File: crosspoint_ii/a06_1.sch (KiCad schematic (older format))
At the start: 44 parts, among them U6001 74HC27, U6002 74HC02, U6003 74HC27, U6004 74LVC07, U6005 74HC02, U6006 74HC04, U6007 74HC27, U6008 74HC27, U6009 74HC02, U6010 74HC04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

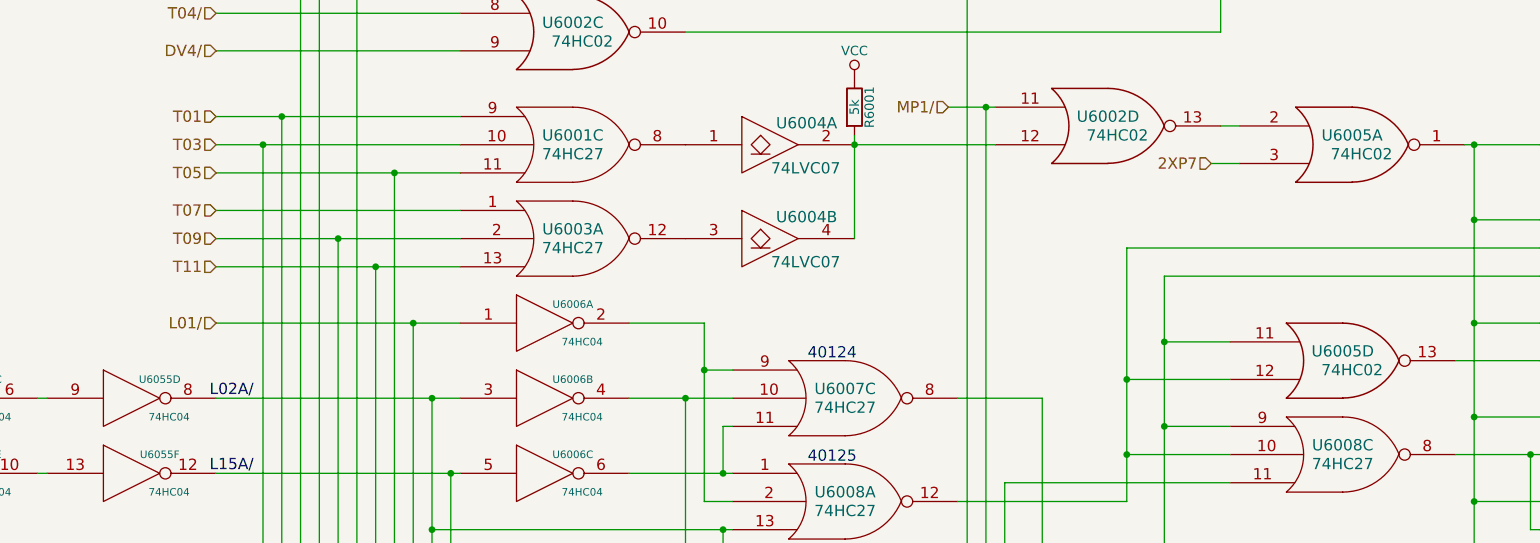
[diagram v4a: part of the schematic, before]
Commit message: Added the final four bit module. All 16 bits of the central/special registers are present. We're stuck at address 0 because TC is using RAD, which needs to be translated into RG or RZ by module 12
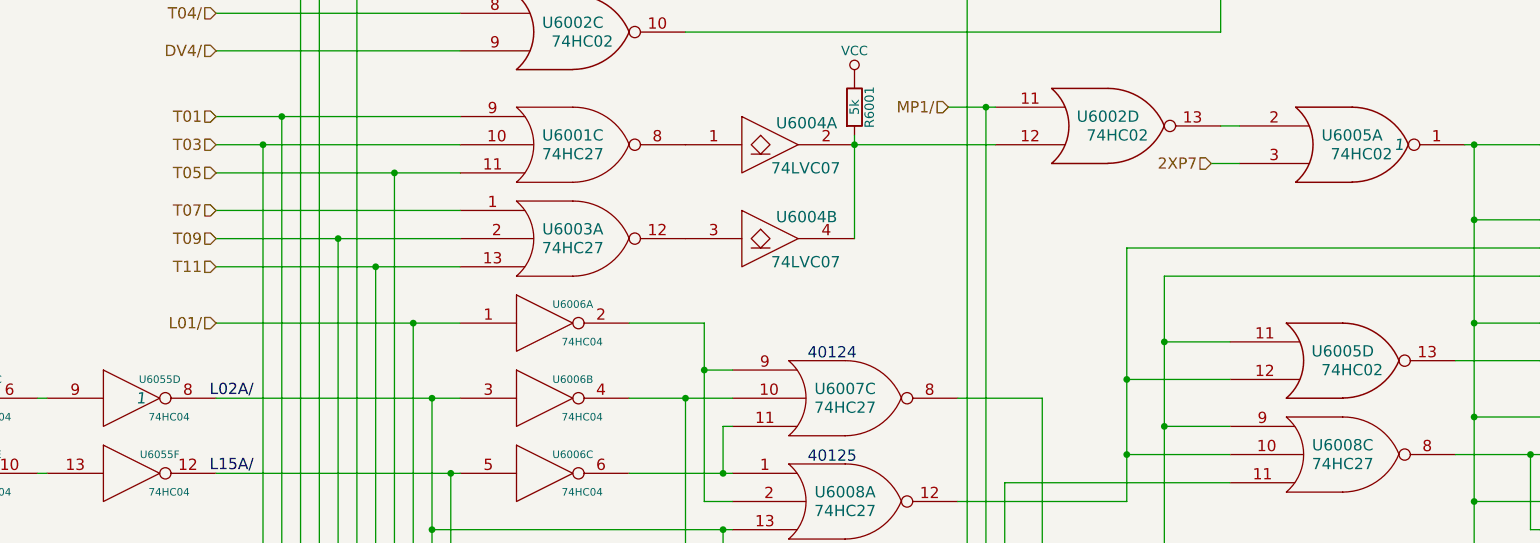
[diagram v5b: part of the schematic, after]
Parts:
- U6005, U6055: Initial (none) -> 1
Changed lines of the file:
@@
 F 2 "" H 9700 3150 60  0000 C CNN
 F 3 "" H 9700 3150 60  0000 C CNN
+F 4 "1" H 9950 3150 60  0000 C CIN "Initial"
 	1    9700 3150
 	1    0    0    -1
@@
 F 2 "" H 3200 4500 60  0000 C CNN
 F 3 "" H 3200 4500 60  0000 C CNN
+F 4 "1" H 3250 4500 60  0000 C CIN "Initial"
 	4    3200 4500
 	1    0    0    -1

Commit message: Added in WHOMP, whatever it is
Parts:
- added U6051: 74HC4002, symbol 74HC4002
- added unit 2 of U6056
- added U6057: 74HC02, symbol 74HC02
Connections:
- net CLXC: now also U6057.3
- net DVXP1: now also U6051.9
- net GND: now also U6051.7 (GND), U6056.7 (GND), U6057.7 (GND)
- net VCC: now also U6051.14 (VCC), U6056.14 (VCC), U6057.14 (VCC)
- new net GOJAM: U6051.10
- new net NISQ: U6051.11
- new net WHOMP: U6051.13, U6057.2
- new net WHOMP/: U6051.12, U6056.3, U6057.1
- new net WHOMPA: U6056.4
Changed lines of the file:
@@
 Connection ~ 12850 12050
-Wire Wire Line
-	11400 2050 11400 1950
-Wire Wire Line
-	11400 1950 11500 1950
-Text HLabel 11500 1950 2    60   Output ~ 0
-DVXP1
 Wire Wire Line
 	6750 6600 6750 6300
@@
 Wire Wire Line
 	16950 6050 16950 6150
-Connection ~ 11400 2050
 Connection ~ 12850 2050
 Wire Wire Line
@@
 Wire Wire Line
 	13200 3700 11900 3700
+Text Label 11350 2050 0    60   ~ 0
+DVXP1
+$Comp
+L 74HC02 U6057
+U 1 1 56AE107E
+P 19700 5750
+F 0 "U6057" H 19700 5800 60  0000 C CNN
+F 1 "74HC02" H 19750 5700 60  0000 C CNN
+F 2 "" H 19700 5750 60  0000 C CNN
+F 3 "" H 19700 5750 60  0000 C CNN
+F 4 "1" H 19950 5750 60  0000 C CIN "Initial"
+	1    19700 5750
+	1    0    0    -1
+$EndComp
+Wire Wire Line
+	20300 5750 20300 5500
+Wire Wire Line
+	20300 5500 19100 5300
+Wire Wire Line
+	19100 5300 19100 5200
+Wire Wire Line
+	20300 5050 20300 5300
+Wire Wire Line
+	20300 5300 19100 5500
+Wire Wire Line
+	19100 5500 19100 5650
+$Comp
+L 74HC4002 U6051
+U 2 1 56AE2757
+P 19700 5050
+F 0 "U6051" H 19700 5100 60  0000 C CNN
+F 1 "74HC4002" H 19750 5000 47  0000 C CNN
+F 2 "" H 19700 5050 60  0000 C CNN
+F 3 "" H 19700 5050 60  0000 C CNN
+	2    19700 5050
+	1    0    0    -1
+$EndComp
+Wire Wire Line
+	17550 7350 17550 7150
+Wire Wire Line
+	17550 7150 18850 7150
+Wire Wire Line
+	18850 7150 18850 5850
+Wire Wire Line
+	18850 5850 19100 5850
+Connection ~ 17550 7350
+Wire Wire Line
+	19100 4900 16850 4900
+Connection ~ 16850 4900
+Text HLabel 19000 5000 0    60   Input ~ 0
+GOJAM
+Wire Wire Line
+	19000 5000 19100 5000
+Text HLabel 19000 5100 0    60   Input ~ 0
+NISQ
+Wire Wire Line
+	19000 5100 19100 5100
+Wire Wire Line
+	20300 5050 20550 5050
+Connection ~ 20300 5050
+Text HLabel 20550 5050 2    60   Output ~ 0
+WHOMP
+Wire Wire Line
+	20300 5750 21000 5750
+Connection ~ 20300 5750
+$Comp
+L 74HC04 U6056
+U 2 1 56AEA36B
+P 21450 5750
+F 0 "U6056" H 21600 5850 40  0000 C CNN
+F 1 "74HC04" H 21650 5650 40  0000 C CNN
+F 2 "" H 21450 5750 60  0000 C CNN
+F 3 "" H 21450 5750 60  0000 C CNN
+	2    21450 5750
+	1    0    0    -1
+$EndComp
+Wire Wire Line
+	21900 5750 22000 5750
+Text HLabel 22000 5750 2    60   Output ~ 0
+WHOMPA
+Text Label 20800 5750 2    60   ~ 0
+WHOMP/
 $EndSCHEMATC

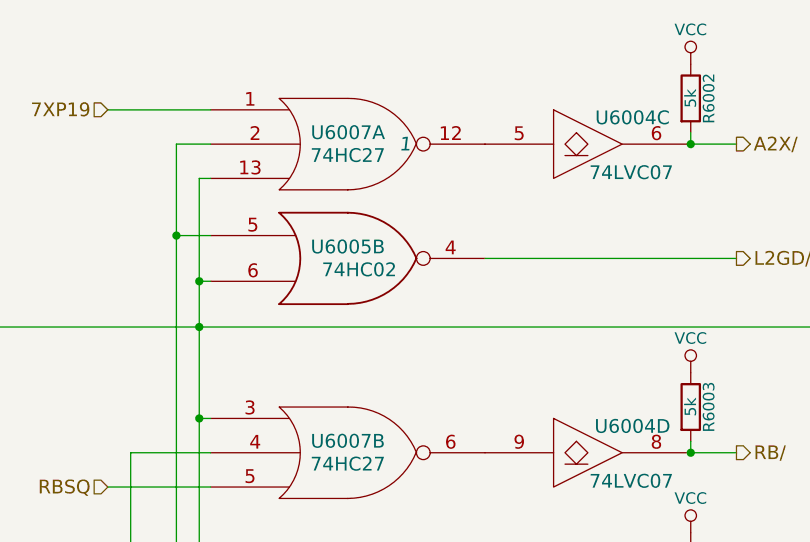
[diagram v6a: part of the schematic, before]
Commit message: Added and tied in module 12, parity & s register
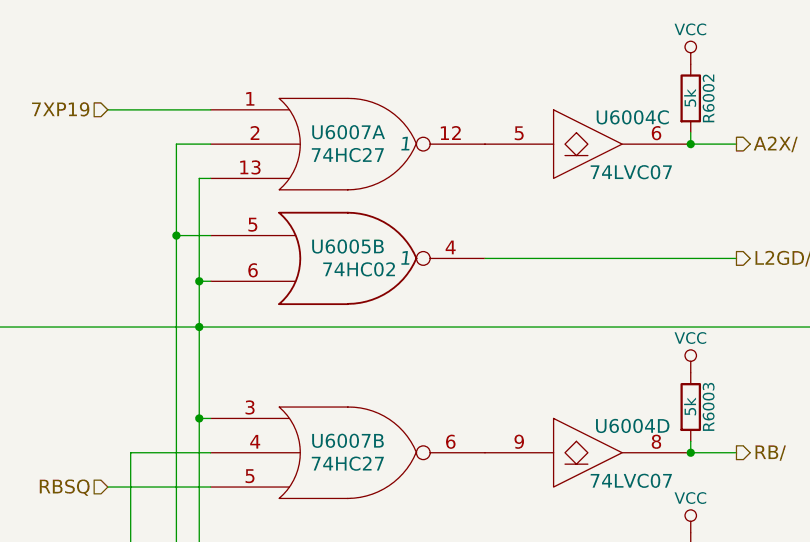
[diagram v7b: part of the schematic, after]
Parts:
- U6005: Initial (none) -> 1
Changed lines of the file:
@@
 F 2 "" H 13500 1750 60  0000 C CNN
 F 3 "" H 13500 1750 60  0000 C CNN
+F 4 "1" H 13750 1750 60  0000 C CIN "Initial"
 	2    13500 1750
 	1    0    0    -1

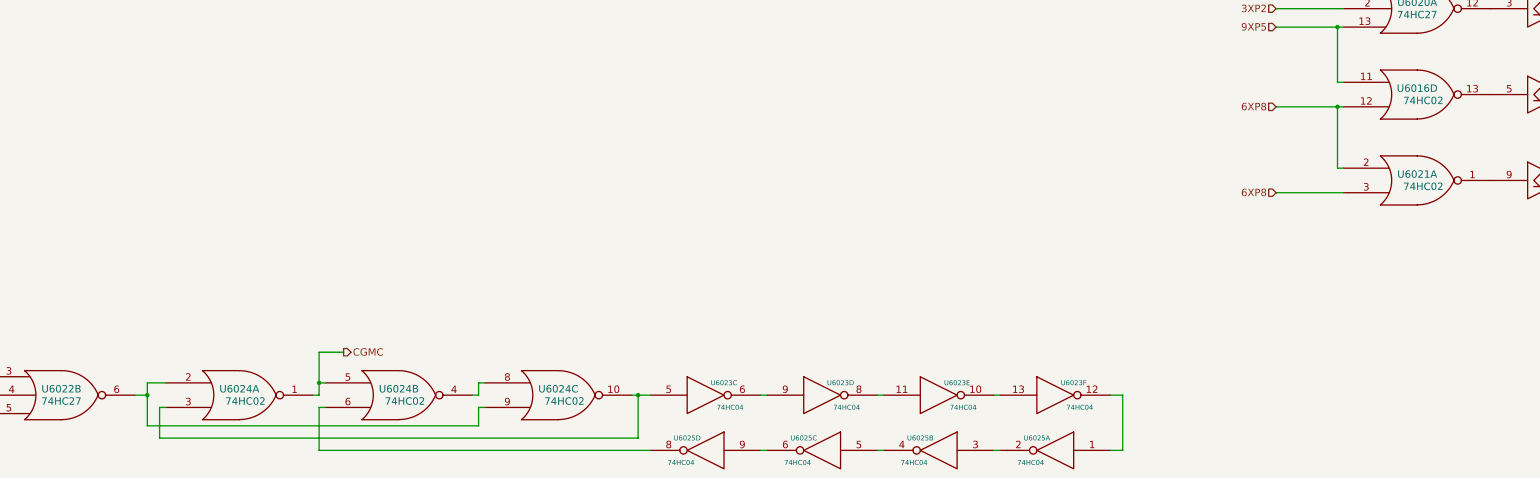
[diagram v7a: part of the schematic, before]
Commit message: Finished off and integrated module 14. Also fixed a couple of bugs this turned up (both initial conditions, and bad wiring in the CGMC pulse generator and S register)
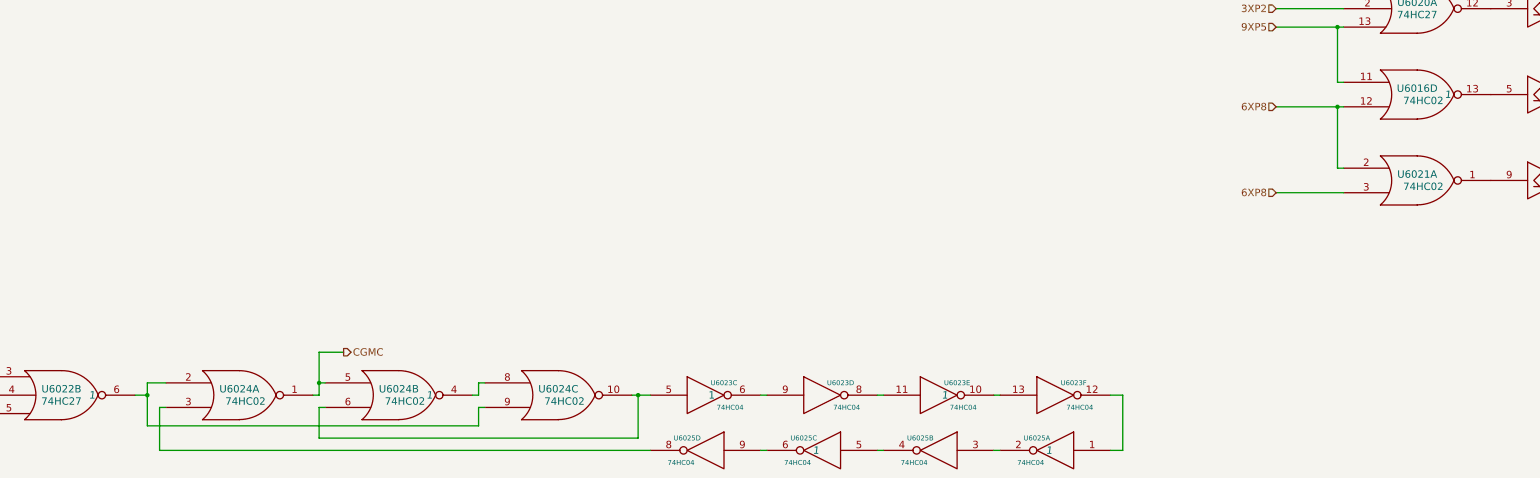
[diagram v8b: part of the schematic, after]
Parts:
- U6016, U6022, U6023, U6024, U6025: Initial (none) -> 1
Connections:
- net at U6023.5, U6024.10: now also U6024.6; no longer U6024.3
- net at U6025.8: now also U6024.3; no longer U6024.6
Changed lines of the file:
@@
 F 2 "" H 13500 11950 60  0000 C CNN
 F 3 "" H 13500 11950 60  0000 C CNN
+F 4 "1" H 13750 11950 60  0000 C CIN "Initial"
 	4    13500 11950
 	1    0    0    -1
@@
 F 2 "" H 2450 14400 60  0000 C CNN
 F 3 "" H 2450 14400 60  0000 C CNN
+F 4 "1" H 2700 14400 60  0000 C CIN "Initial"
 	2    2450 14400
 	1    0    0    -1
@@
 	3050 14400 3150 14400
 Wire Wire Line
-	3150 14300 3150 14650
-Wire Wire Line
 	3150 14300 3300 14300
 $Comp
@@
 F 2 "" H 5200 14400 60  0000 C CNN
 F 3 "" H 5200 14400 60  0000 C CNN
+F 4 "1" H 5450 14400 60  0000 C CIN "Initial"
 	2    5200 14400
 	1    0    0    -1
@@
 F 2 "" H 7700 14400 60  0000 C CNN
 F 3 "" H 7700 14400 60  0000 C CNN
+F 4 "1" H 7750 14400 60  0000 C CNN "Initial"
 	3    7700 14400
 	1    0    0    -1
@@
 F 2 "" H 9600 14400 60  0000 C CNN
 F 3 "" H 9600 14400 60  0000 C CNN
+F 4 "1" H 9650 14400 60  0000 C CIN "Initial"
 	5    9600 14400
 	1    0    0    -1
@@
 F 2 "" H 10550 14850 60  0000 C CNN
 F 3 "" H 10550 14850 60  0000 C CNN
+F 4 "1" H 10600 14850 60  0000 C CIN "Initial"
 	1    10550 14850
 	-1   0    0    -1
@@
 F 2 "" H 8650 14850 60  0000 C CNN
 F 3 "" H 8650 14850 60  0000 C CNN
+F 4 "1" H 8700 14850 60  0000 C CIN "Initial"
 	3    8650 14850
 	-1   0    0    -1
@@
 Connection ~ 4550 14300
 Wire Wire Line
-	7250 14850 4550 14850
-Wire Wire Line
-	4550 14850 4550 14500
-Wire Wire Line
-	4550 14500 4600 14500
-Wire Wire Line
-	7150 14400 7150 14750
-Wire Wire Line
-	7150 14750 3250 14750
-Wire Wire Line
-	3250 14750 3250 14500
-Wire Wire Line
 	3250 14500 3300 14500
 Connection ~ 7150 14400
-Wire Wire Line
-	3150 14650 5850 14650
-Wire Wire Line
-	5850 14650 5850 14500
 Wire Wire Line
 	5850 14500 5900 14500
@@
 Text Label 20800 5750 2    60   ~ 0
 WHOMP/
+Wire Wire Line
+	3150 14300 3150 14650
+Wire Wire Line
+	7250 14850 3250 14850
+Wire Wire Line
+	3250 14850 3250 14500
+Wire Wire Line
+	3150 14650 5850 14650
+Wire Wire Line
+	5850 14650 5850 14500
+Wire Wire Line
+	4600 14500 4550 14500
+Wire Wire Line
+	4550 14500 4550 14750
+Wire Wire Line
+	4550 14750 7150 14750
+Wire Wire Line
+	7150 14750 7150 14400
 $EndSCHEMATC
